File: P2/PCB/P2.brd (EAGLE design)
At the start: 98.7 x 30.5 mm, 32 parts, among them CON1 Volume, CON2 Autosense, CON3 Noritake, IC1 ATMEGA48/88/168-AU, IC2 TPIC6B595DW, IC3 TPIC6B595DW, K1 G6H2-100, Q1 16MHz

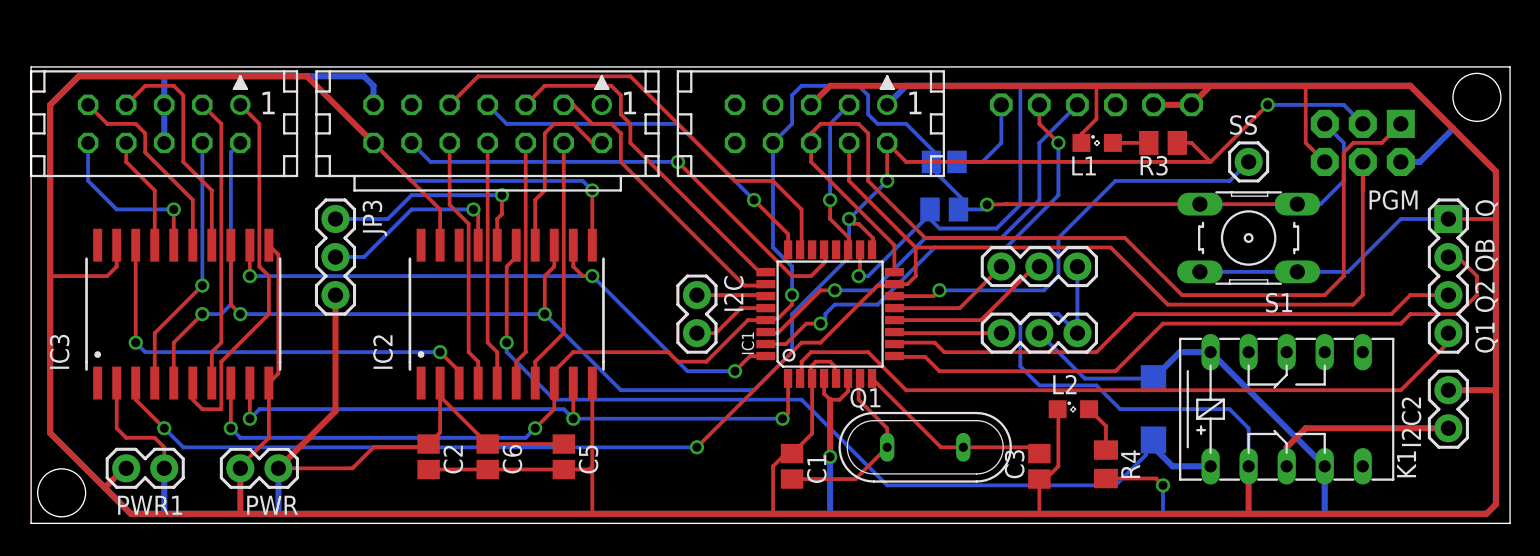
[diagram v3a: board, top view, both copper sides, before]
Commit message: Added AREF Jumper
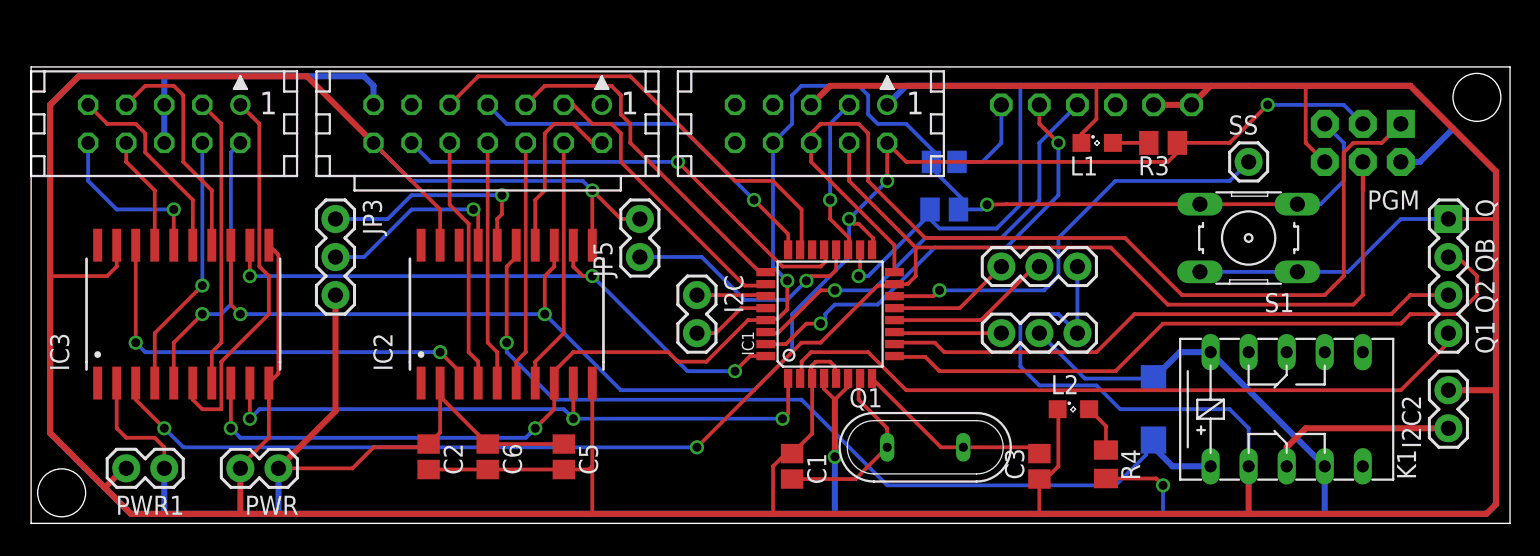
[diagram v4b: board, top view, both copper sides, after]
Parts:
- added JP5: aref, SparkFun:1X02
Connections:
- new net N$13: IC1.20, JP5.1
- net GND: now also JP5.2
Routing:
- net N$13: track 0.00 -> 16.5 mm, vias 0 -> 1
- net GND: track 386.8 -> 390.8 mm
- net SCK: track 106.4 -> 104.0 mm
- net AGND: track 32.5 -> 32.0 mm
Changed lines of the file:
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@@
 <attribute name="NAME" x="79.9338" y="25.9588" size="1.27" layer="25"/>
 </element>
+<element name="JP5" library="SparkFun" package="1X02" value="aref" x="40.64" y="17.78" rot="R90"/>
 </elements>
 <signals>
@@
 <wire x1="80.01" y1="7.62" x2="81.28" y2="6.35" width="0.254" layer="16"/>
 <wire x1="81.28" y1="6.35" x2="81.28" y2="3.81" width="0.254" layer="16"/>
+<contactref element="JP5" pad="2"/>
+<wire x1="40.64" y1="20.32" x2="39.37" y2="20.32" width="0.254" layer="1"/>
+<wire x1="39.37" y1="20.32" x2="37.465" y2="22.225" width="0.254" layer="1"/>
 </signal>
 <signal name="+5V">
@@
 <wire x1="8.89" y1="25.4" x2="8.89" y2="27.94" width="0.4064" layer="16"/>
 <wire x1="8.89" y1="0.635" x2="16.51" y2="0.635" width="0.4064" layer="16"/>
-<wire x1="16.51" y1="0.635" x2="53.34" y2="0.635" width="0.4064" layer="16"/>
-<wire x1="53.34" y1="0.635" x2="75.565" y2="0.635" width="0.4064" layer="16"/>
+<wire x1="16.51" y1="0.635" x2="53.6575" y2="0.635" width="0.4064" layer="16"/>
+<wire x1="53.6575" y1="0.635" x2="75.565" y2="0.635" width="0.4064" layer="16"/>
 <wire x1="75.565" y1="0.635" x2="86.36" y2="0.635" width="0.4064" layer="16"/>
 <wire x1="8.89" y1="3.675" x2="8.89" y2="0.635" width="0.4064" layer="16"/>
@@
 <wire x1="27.305" y1="8.47" x2="27.305" y2="6.065" width="0.254" layer="1"/>
 <wire x1="27.305" y1="6.065" x2="26.535" y2="5.295" width="0.254" layer="1"/>
-<wire x1="53.34" y1="0.635" x2="53.34" y2="4.445" width="0.4064" layer="16"/>
-<via x="53.34" y="4.445" extent="1-16" drill="0.6"/>
+<wire x1="53.6575" y1="0.635" x2="53.6575" y2="4.445" width="0.4064" layer="16"/>
+<via x="53.6575" y="4.445" extent="1-16" drill="0.6"/>
 <wire x1="75.565" y1="0.635" x2="75.565" y2="2.54" width="0.254" layer="16"/>
 <via x="75.565" y="2.54" extent="1-16" drill="0.6"/>
@@
 <wire x1="71.755" y1="2.995" x2="75.11" y2="2.995" width="0.254" layer="1"/>
 <wire x1="75.11" y1="2.995" x2="75.565" y2="2.54" width="0.254" layer="1"/>
-<wire x1="53.34" y1="4.445" x2="53.34" y2="8.255" width="0.4064" layer="1"/>
-<wire x1="54.54" y1="9.6774" x2="54.54" y2="8.82" width="0.254" layer="1"/>
-<wire x1="54.54" y1="8.82" x2="53.975" y2="8.255" width="0.254" layer="1"/>
-<wire x1="53.975" y1="8.255" x2="53.34" y2="8.255" width="0.254" layer="1"/>
-<wire x1="52.94" y1="9.6774" x2="52.94" y2="8.655" width="0.254" layer="1"/>
-<wire x1="52.94" y1="8.655" x2="53.34" y2="8.255" width="0.254" layer="1"/>
+<wire x1="53.6575" y1="4.445" x2="53.6575" y2="8.255" width="0.4064" layer="1"/>
 <wire x1="1.27" y1="27.94" x2="1.27" y2="6.0325" width="0.4064" layer="16"/>
 <wire x1="1.27" y1="6.0325" x2="6.6675" y2="0.635" width="0.4064" layer="16"/>
@@
 <wire x1="59.69" y1="20.32" x2="55.88" y2="16.51" width="0.254" layer="16"/>
 <wire x1="55.88" y1="16.51" x2="55.245" y2="16.51" width="0.254" layer="16"/>
+<wire x1="52.94" y1="9.6774" x2="52.94" y2="8.9725" width="0.254" layer="1"/>
+<wire x1="52.94" y1="8.9725" x2="53.6575" y2="8.255" width="0.254" layer="1"/>
+<wire x1="54.54" y1="9.6774" x2="54.54" y2="9.1375" width="0.254" layer="1"/>
+<wire x1="54.54" y1="9.1375" x2="53.6575" y2="8.255" width="0.254" layer="1"/>
 </signal>
 <signal name="MOSI">
@@
 <via x="13.97" y="13.97" extent="1-16" drill="0.6"/>
 <wire x1="88.9" y1="26.67" x2="87.63" y2="27.94" width="0.254" layer="16"/>
-<wire x1="78.74" y1="24.13" x2="58.42" y2="24.13" width="0.254" layer="1"/>
 <wire x1="58.42" y1="24.13" x2="57.15" y2="25.4" width="0.254" layer="1"/>
 <via x="57.15" y="22.86" extent="1-16" drill="0.6" shape="octagon"/>
@@
 <wire x1="54.9275" y1="20.0025" x2="54.61" y2="20.32" width="0.254" layer="1"/>
 <wire x1="87.63" y1="27.94" x2="82.55" y2="27.94" width="0.254" layer="16"/>
-<wire x1="82.55" y1="27.94" x2="78.74" y2="24.13" width="0.254" layer="1"/>
-<wire x1="76.515" y1="25.4" x2="77.47" y2="25.4" width="0.254" layer="1"/>
-<wire x1="77.47" y1="25.4" x2="78.74" y2="24.13" width="0.254" layer="1"/>
+<wire x1="82.55" y1="27.94" x2="80.01" y2="25.4" width="0.254" layer="1"/>
 <via x="82.55" y="27.94" extent="1-16" drill="0.6"/>
+<wire x1="76.515" y1="25.4" x2="80.01" y2="25.4" width="0.254" layer="1"/>
+<wire x1="58.42" y1="24.13" x2="75.8825" y2="24.13" width="0.254" layer="1"/>
+<wire x1="75.8825" y1="24.13" x2="76.5175" y2="24.765" width="0.254" layer="1"/>
+<wire x1="76.5175" y1="24.765" x2="76.5175" y2="25.3975" width="0.254" layer="1"/>
+<wire x1="76.5175" y1="25.3975" x2="76.515" y2="25.4" width="0.254" layer="1"/>
 </signal>
 <signal name="SS">
@@
 <wire x1="86.36" y1="26.67" x2="87.63" y2="25.4" width="0.254" layer="16"/>
 <wire x1="50.8" y1="26.67" x2="49.53" y2="25.4" width="0.254" layer="16"/>
-<wire x1="49.53" y1="25.4" x2="49.53" y2="18.415" width="0.254" layer="16"/>
-<wire x1="49.53" y1="18.415" x2="50.8" y2="17.145" width="0.254" layer="16"/>
+<wire x1="49.53" y1="25.4" x2="49.53" y2="17.145" width="0.254" layer="16"/>
 <wire x1="87.63" y1="25.4" x2="87.63" y2="22.86" width="0.254" layer="16"/>
 <wire x1="87.63" y1="22.86" x2="86.0806" y2="21.3106" width="0.254" layer="16"/>
@@
 <via x="63.8175" y="21.2725" extent="1-16" drill="0.6"/>
 <wire x1="78.0288" y1="21.3106" x2="65.1256" y2="21.3106" width="0.254" layer="1"/>
-<wire x1="50.8" y1="17.145" x2="50.8" y2="15.24" width="0.254" layer="16"/>
-<via x="50.8" y="15.24" extent="1-16" drill="0.6"/>
+<via x="50.4825" y="16.1925" extent="1-16" drill="0.6"/>
 <contactref element="IC2" pad="8"/>
 <contactref element="IC3" pad="8"/>
@@
 <wire x1="42.545" y1="11.43" x2="43.18" y2="10.795" width="0.254" layer="1"/>
 <wire x1="43.18" y1="10.795" x2="45.085" y2="10.795" width="0.254" layer="1"/>
-<wire x1="50.8" y1="15.24" x2="50.8" y2="14.605" width="0.254" layer="1"/>
-<wire x1="50.8" y1="14.605" x2="49.8475" y2="13.6525" width="0.254" layer="1"/>
 <wire x1="49.8475" y1="13.6525" x2="49.1299" y2="13.6525" width="0.254" layer="1"/>
 <wire x1="49.1299" y1="13.6525" x2="49.0474" y2="13.57" width="0.254" layer="1"/>
@@
 <wire x1="61.91" y1="20.955" x2="63.5" y2="20.955" width="0.254" layer="16"/>
 <wire x1="63.5" y1="20.955" x2="63.8175" y2="21.2725" width="0.254" layer="16"/>
+<wire x1="49.8475" y1="13.6525" x2="50.4825" y2="14.2875" width="0.254" layer="1"/>
+<wire x1="50.4825" y1="14.2875" x2="50.4825" y2="16.1925" width="0.254" layer="1"/>
+<wire x1="49.53" y1="17.145" x2="50.4825" y2="16.1925" width="0.254" layer="16"/>
 </signal>
 <signal name="QE1">
@@
 <contactref element="CON2" pad="12"/>
 <contactref element="IC1" pad="21"/>
-<wire x1="50.8" y1="16.51" x2="52.07" y2="16.51" width="0.254" layer="1"/>
-<wire x1="52.07" y1="16.51" x2="53.0225" y2="17.4625" width="0.254" layer="1"/>
 <wire x1="25.4" y1="25.4" x2="26.67" y2="24.13" width="0.254" layer="16"/>
 <wire x1="26.67" y1="24.13" x2="43.18" y2="24.13" width="0.254" layer="16"/>
-<wire x1="43.18" y1="24.13" x2="50.8" y2="16.51" width="0.254" layer="1"/>
 <via x="43.18" y="24.13" extent="1-16" drill="0.6"/>
 <wire x1="53.0225" y1="17.4625" x2="53.0225" y2="18.1801" width="0.254" layer="1"/>
 <wire x1="53.0225" y1="18.1801" x2="52.94" y2="18.2626" width="0.254" layer="1"/>
+<wire x1="53.0225" y1="17.4625" x2="52.705" y2="17.145" width="0.254" layer="1"/>
+<wire x1="52.705" y1="17.145" x2="50.165" y2="17.145" width="0.254" layer="1"/>
+<wire x1="50.165" y1="17.145" x2="43.18" y2="24.13" width="0.254" layer="1"/>
 </signal>
 <signal name="N$3">
@@
 <wire x1="66.9925" y1="16.8275" x2="67.31" y2="17.145" width="0.254" layer="1"/>
 </signal>
+<signal name="N$13">
+<contactref element="JP5" pad="1"/>
+<contactref element="IC1" pad="20"/>
+<wire x1="53.74" y1="18.2626" x2="53.74" y2="16.91" width="0.254" layer="1"/>
+<wire x1="51.7525" y1="16.1925" x2="50.4825" y2="14.9225" width="0.254" layer="16"/>
+<wire x1="50.4825" y1="14.9225" x2="47.625" y2="14.9225" width="0.254" layer="16"/>
+<wire x1="47.625" y1="14.9225" x2="44.7675" y2="17.78" width="0.254" layer="16"/>
+<wire x1="44.7675" y1="17.78" x2="40.64" y2="17.78" width="0.254" layer="16"/>
+<wire x1="53.74" y1="16.91" x2="53.34" y2="16.51" width="0.254" layer="1"/>
+<wire x1="53.34" y1="16.51" x2="52.07" y2="16.51" width="0.254" layer="1"/>
+<wire x1="52.07" y1="16.51" x2="51.7525" y2="16.1925" width="0.254" layer="1"/>
+<via x="51.7525" y="16.1925" extent="1-16" drill="0.6"/>
+</signal>
 </signals>
